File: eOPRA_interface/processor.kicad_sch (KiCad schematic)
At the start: 50 parts, among them SW1 SW_Push, U10 RP2040, U11 W25Q128JVP, U13 MCP25625, Y1 16Mhz 12pF, Y3 12Mhz 12pF

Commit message: stuff
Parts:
- added C10: 0.1uF, 2_Passives_Capacitors_SMD_IPC:C_1005_402_A, symbol 2.passive:C
- added NT3: net-tie, 0_NetTie:NetTie-2_SMD_Pad0.5mm, symbol 0.power-symbols:net-tie
- C21, C22, C4, C5: PN 2,2 -> 2,4
- R13, R14: value 27k4 -> 27.4
- R81: footprint 2_Passives_Resistors_SMD_IPC:R_1608_603_B -> 2_Passives_Resistors_SMD_IPC:R_1005_402_A
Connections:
- net +3V3: now also C10.2
- net GND: now also NT3.2; no longer C21.2, C22.1, C23.1, C24.1, C33.2, D1.3 (common), R15.2, U13.18 (VSS), U13.22 (GND), U13.29 (EP), Y1.2, Y1.4
- new net GNDISO2: C10.1, C21.2, C22.1, C23.1, C24.1, C33.2, D1.3 (common), NT3.1, R15.2, U13.18 (VSS), U13.22 (GND), U13.29 (EP), Y1.2, Y1.4
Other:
- moved on the sheet: C21, C22, C23, C24, C33, D1, JP4, R11, R15, R25, R80, R81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

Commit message: stuffs
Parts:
- C23, C24: now not fitted
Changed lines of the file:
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@@
   )
   (symbol (lib_id "2.passive:C") (at 394.335 132.08 180) (unit 1)
-    (in_bom yes) (on_board yes) (dnp no)
+    (in_bom yes) (on_board yes) (dnp yes)
     (property "Reference" "C24" (at 387.35 131.429 0)
       (effects (font (size 1.27 1.27)) (justify right))
@@
   )
   (symbol (lib_id "2.passive:C") (at 375.285 132.08 180) (unit 1)
-    (in_bom yes) (on_board yes) (dnp no)
+    (in_bom yes) (on_board yes) (dnp yes)
     (property "Reference" "C23" (at 368.3 131.429 0)
       (effects (font (size 1.27 1.27)) (justify right))

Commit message: initial state
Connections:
- net A_IN_2_PIN: no longer U10.38 (GPIO26_ADC0)
- new net SWITCH_CTL: U10.38 (GPIO26_ADC0)
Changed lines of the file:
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@@
     (effects (font (size 1.27 1.27)) (justify right bottom))
-  )
-  (label "A_IN_2_PIN" (at 226.06 170.815 0) (fields_autoplaced)
-    (effects (font (size 1.27 1.27)) (justify left bottom))
   )
   (label "QSPI_SD3" (at 80.01 154.305 0) (fields_autoplaced)
@@
     (effects (font (size 1.27 1.27)) (justify right))
   )
+  (hierarchical_label "SWITCH_CTL" (shape output) (at 226.06 170.815 0) (fields_autoplaced)
+    (effects (font (size 1.27 1.27)) (justify left))
+  )
   (hierarchical_label "SCL1" (shape bidirectional) (at 226.06 150.495 0) (fields_autoplaced)

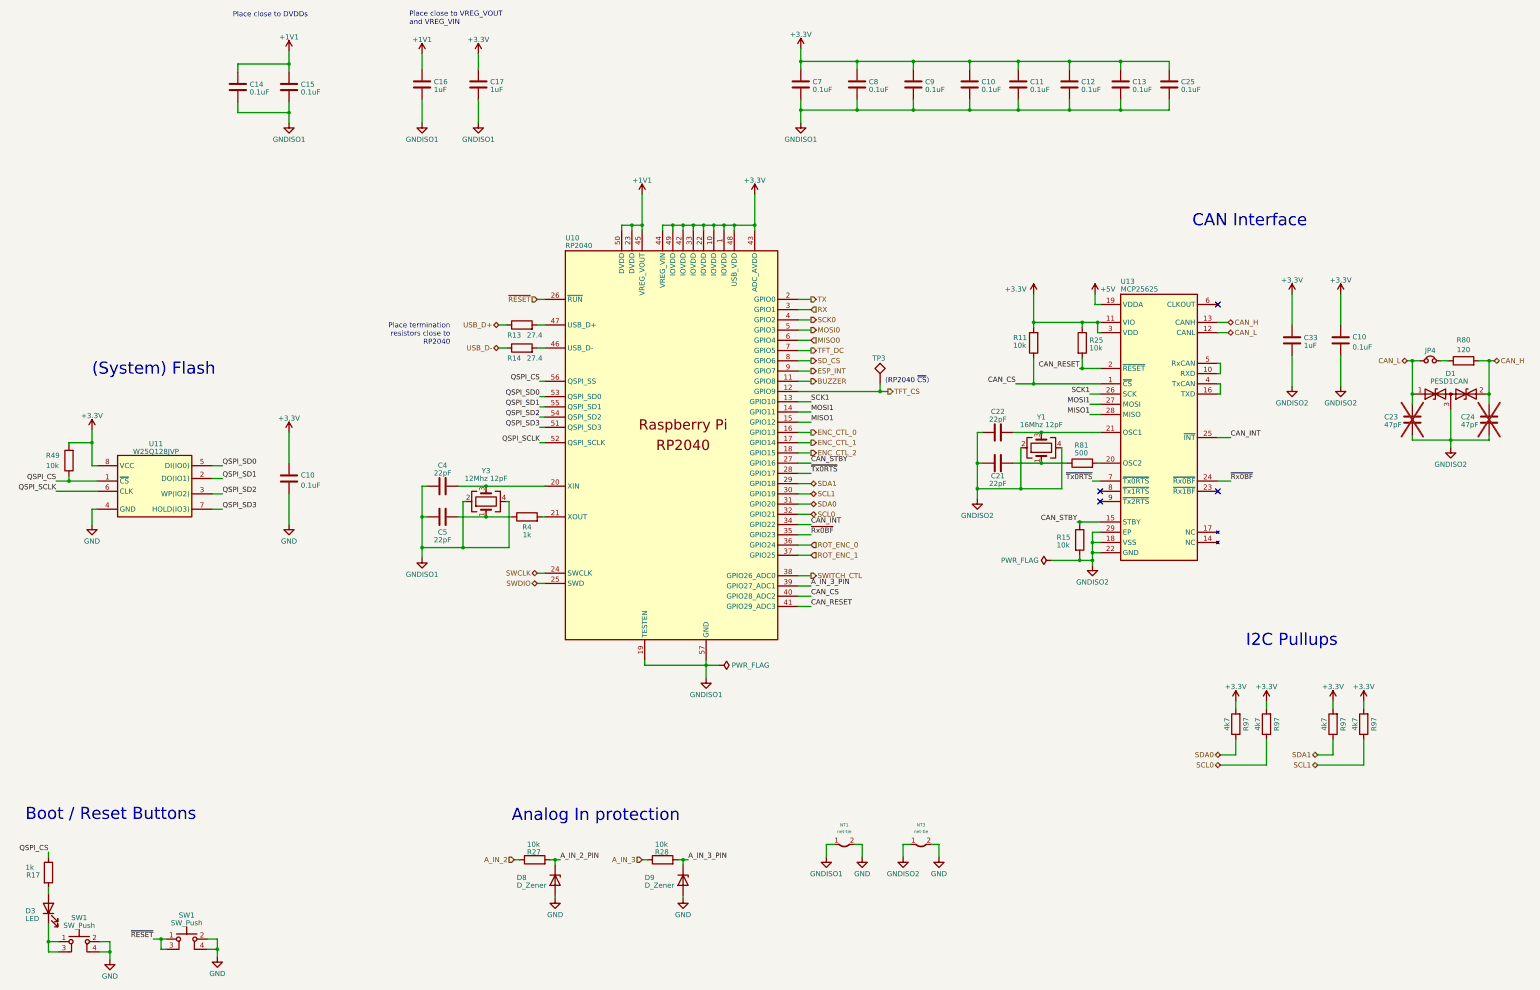
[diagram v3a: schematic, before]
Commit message: switch port on interrupt
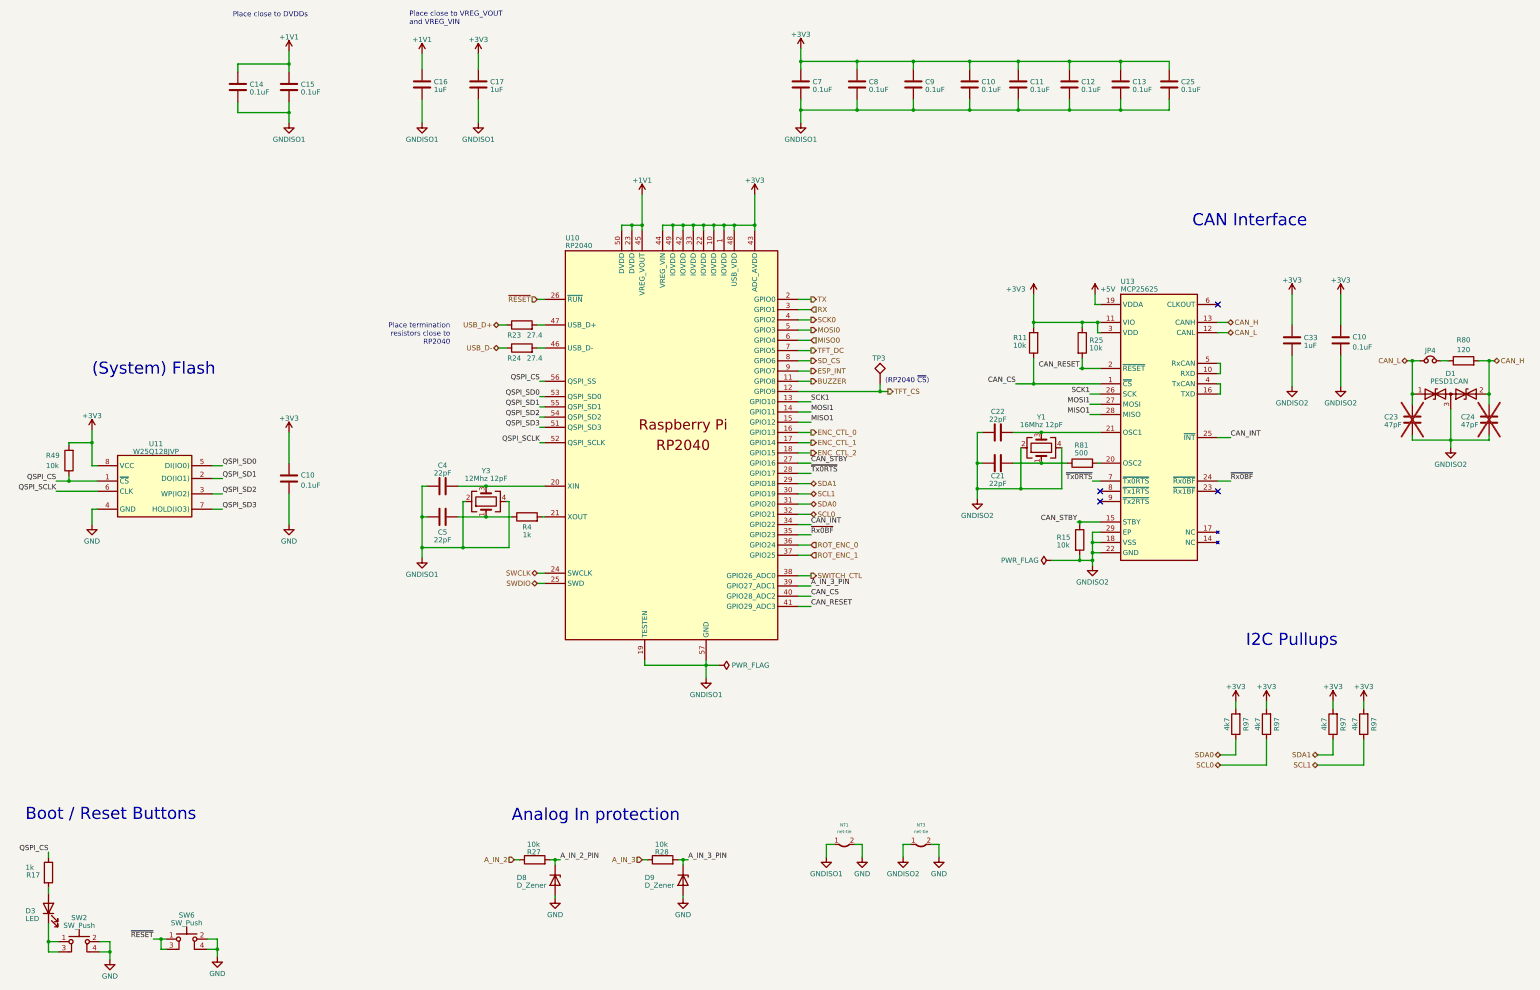
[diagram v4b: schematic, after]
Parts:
- renumbered R13 to R23, R14 to R24, SW1 to SW2, SW1 to SW6
